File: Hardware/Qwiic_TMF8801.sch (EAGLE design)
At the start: 22 parts, among them J1 QWIIC_RIGHT_ANGLE, J2 QWIIC_RIGHT_ANGLE, U1 TMF8801

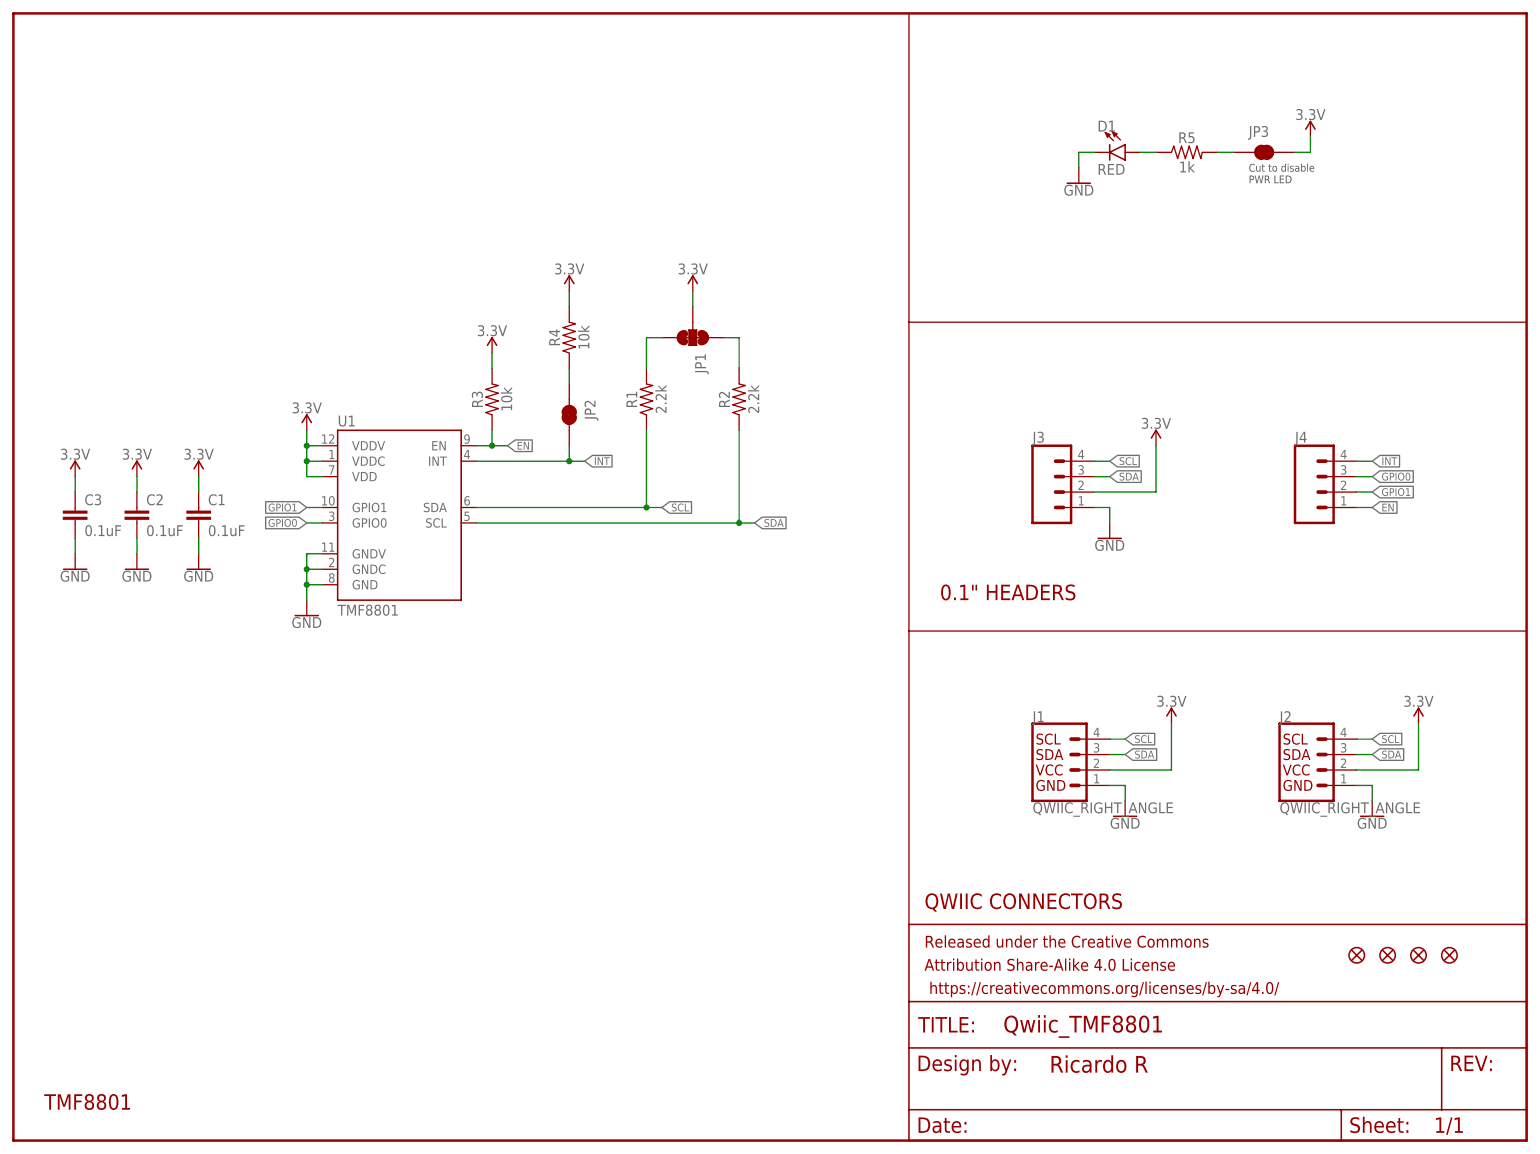
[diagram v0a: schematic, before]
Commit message: Layout changes
Changed board layout per Nathan's feedback.
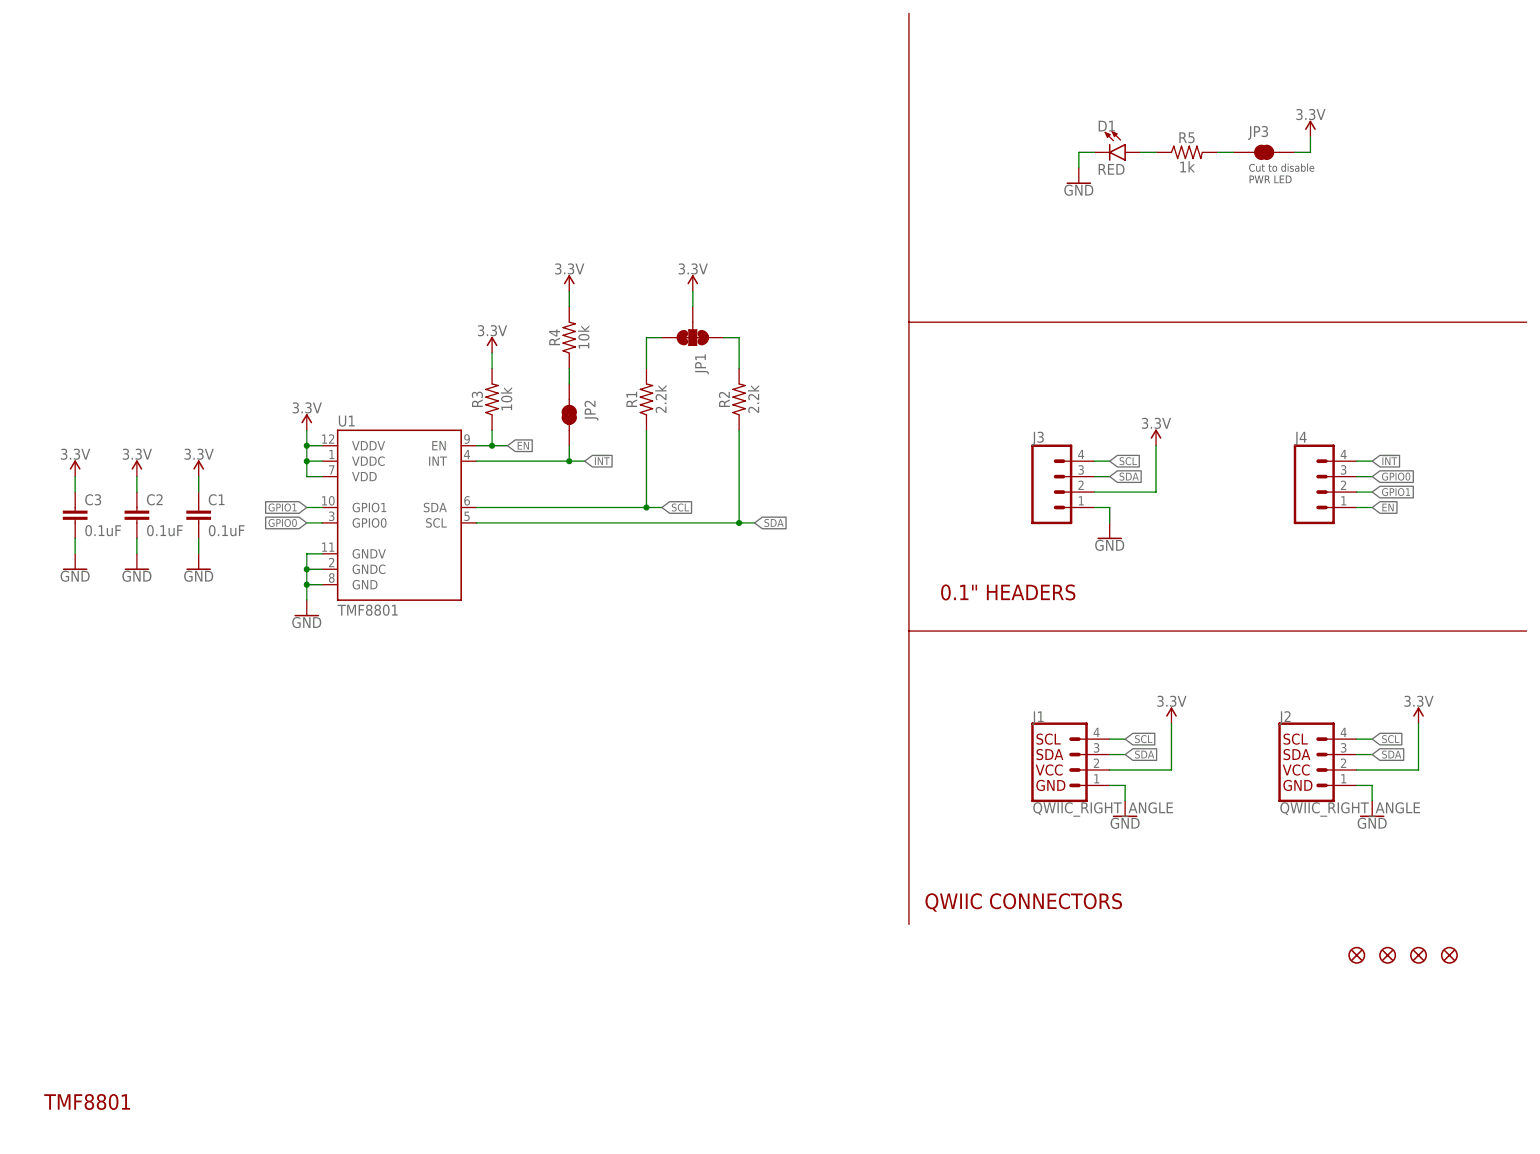
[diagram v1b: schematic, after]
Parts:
- removed FRAME1: FRAME-LETTERNO_PACKAGE, SparkFun-Aesthetics:FRAME-LETTERNO_PACKAGE
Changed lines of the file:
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@@
 <part name="FD3" library="SparkFun-Aesthetics" deviceset="FIDUCIAL" device="1X2"/>
 <part name="FD4" library="SparkFun-Aesthetics" deviceset="FIDUCIAL" device="1X2"/>
-<part name="FRAME1" library="SparkFun-Aesthetics" deviceset="FRAME-LETTER" device="NO_PACKAGE">
-<attribute name="DESIGNER" value="Ricardo R"/>
-</part>
 </parts>
 <sheets>
@@
 <instance part="FD3" gate="G$1" x="220.98" y="30.48" smashed="yes"/>
 <instance part="FD4" gate="G$1" x="226.06" y="30.48" smashed="yes"/>
-<instance part="FRAME1" gate="G$1" x="0" y="0" smashed="yes"/>
-<instance part="FRAME1" gate="V" x="147.32" y="0" smashed="yes">
-<attribute name="LAST_DATE_TIME" x="160.02" y="1.27" size="2.54" layer="94" font="vector"/>
-<attribute name="SHEET" x="233.68" y="1.27" size="2.54" layer="94" font="vector"/>
-<attribute name="DRAWING_NAME" x="162.814" y="17.78" size="2.7432" layer="94" font="vector"/>
-<attribute name="DESIGNER" x="170.434" y="11.176" size="2.7432" layer="94" font="vector"/>
-</instance>
 </instances>
 <busses>

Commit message: Added missing frame to schematic; removed extra fiducial
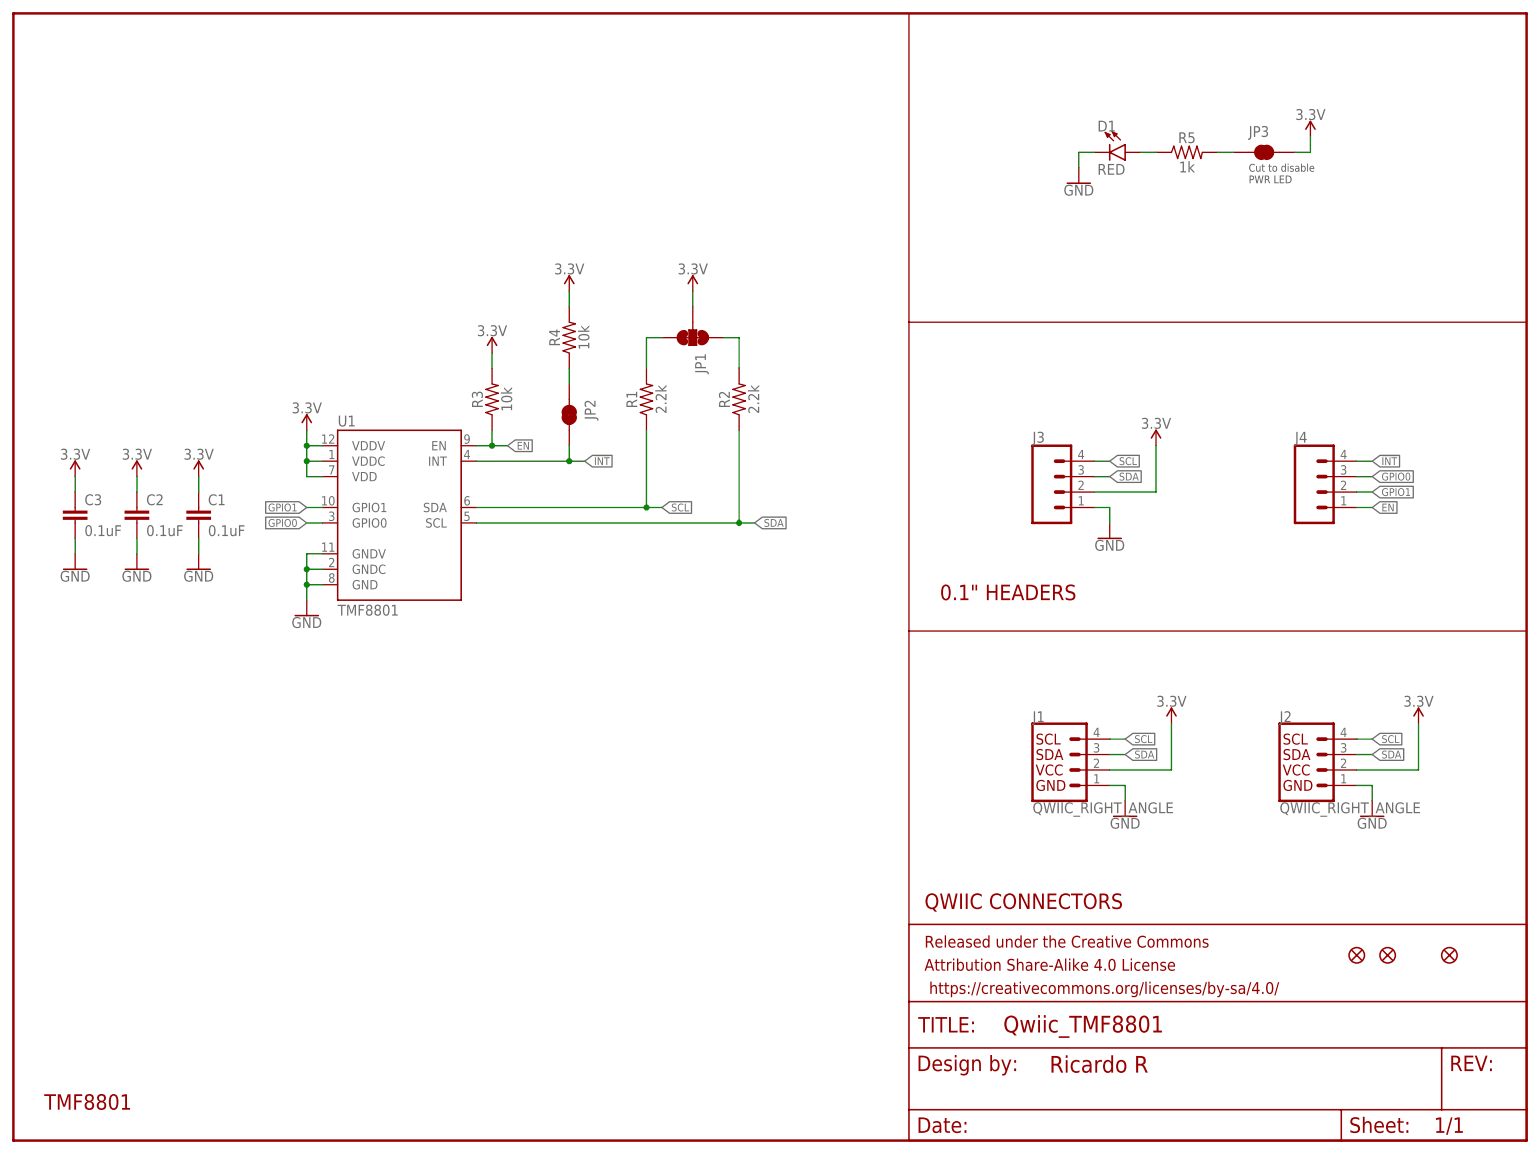
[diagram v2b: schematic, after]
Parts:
- removed FD2: FIDUCIAL1X2, SparkFun-Aesthetics:FIDUCIAL1X2
- added FRAME1: FRAME-LETTERNO_PACKAGE, SparkFun-Aesthetics:FRAME-LETTERNO_PACKAGE
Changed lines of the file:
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@@
 <part name="R4" library="SparkFun-Resistors" deviceset="10KOHM" device="-0603-1/10W-1%" value="10k"/>
 <part name="FD1" library="SparkFun-Aesthetics" deviceset="FIDUCIAL" device="1X2"/>
-<part name="FD2" library="SparkFun-Aesthetics" deviceset="FIDUCIAL" device="1X2"/>
 <part name="FD3" library="SparkFun-Aesthetics" deviceset="FIDUCIAL" device="1X2"/>
 <part name="FD4" library="SparkFun-Aesthetics" deviceset="FIDUCIAL" device="1X2"/>
+<part name="FRAME1" library="SparkFun-Aesthetics" deviceset="FRAME-LETTER" device="NO_PACKAGE">
+<attribute name="DESIGNER" value="Ricardo R"/>
+</part>
 </parts>
 <sheets>
@@
 </instance>
 <instance part="FD1" gate="G$1" x="236.22" y="30.48" smashed="yes"/>
-<instance part="FD2" gate="G$1" x="231.14" y="30.48" smashed="yes"/>
 <instance part="FD3" gate="G$1" x="220.98" y="30.48" smashed="yes"/>
 <instance part="FD4" gate="G$1" x="226.06" y="30.48" smashed="yes"/>
+<instance part="FRAME1" gate="G$1" x="0" y="0" smashed="yes"/>
+<instance part="FRAME1" gate="V" x="147.32" y="0" smashed="yes">
+<attribute name="LAST_DATE_TIME" x="160.02" y="1.27" size="2.54" layer="94" font="vector"/>
+<attribute name="SHEET" x="233.68" y="1.27" size="2.54" layer="94" font="vector"/>
+<attribute name="DRAWING_NAME" x="162.814" y="17.78" size="2.7432" layer="94" font="vector"/>
+<attribute name="DESIGNER" x="170.434" y="11.176" size="2.7432" layer="94" font="vector"/>
+</instance>
 </instances>
 <busses>
